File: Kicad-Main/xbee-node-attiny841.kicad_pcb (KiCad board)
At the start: 2 copper layers, 58.5 x 58.5 mm, 44 parts, among them P10 CONN_1, P11 CONN_1, P12 CONN_1, P13 CONN_1, P14 CONN_1, P15 CONN_1, P16 CONN_1, P17 CONN_1, P18 CONN_1, P19 CONN_1, P2 XBee Adaptor, P3 Test, P4 Battery, P5 XBee-ext-1, P6 XBee-ext-2, P7 CONN_1, P8 CONN_1, P9 CONN_1, Q2 S9014, Q3 2N7000, U1 ATTINY84-S, U2 MAX952ESA, U3 TPS77033, U4 TPS77033

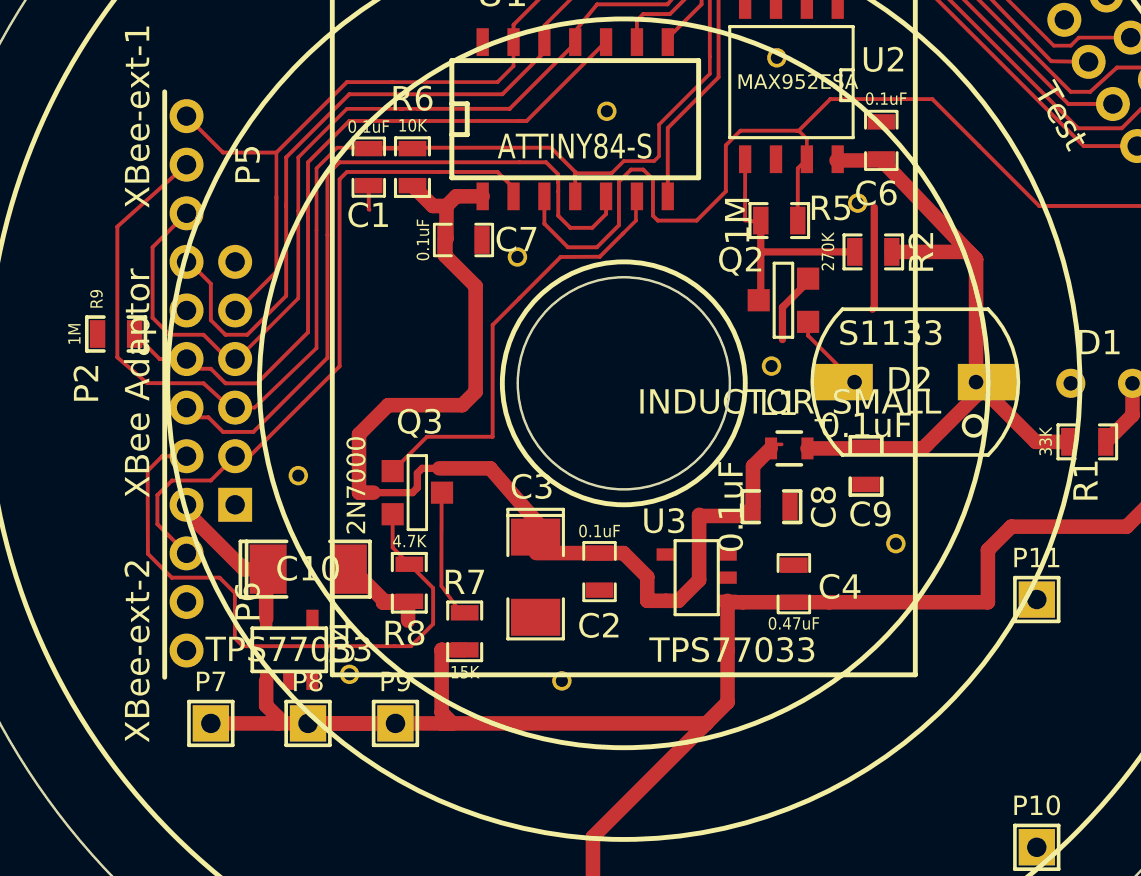
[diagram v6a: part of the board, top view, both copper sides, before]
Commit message: Change PCBs to move XBee regulator and caps to the mount board. Change Vcc on mount board to take full battery voltage.
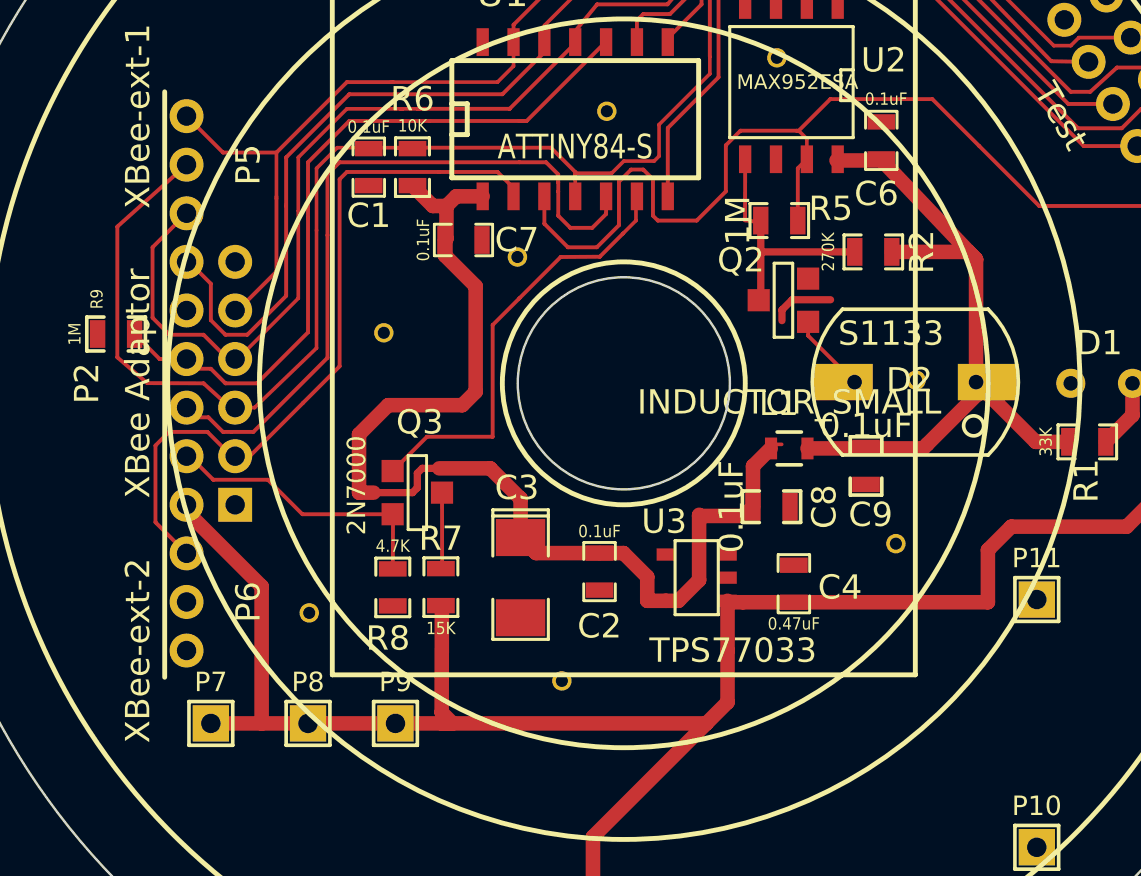
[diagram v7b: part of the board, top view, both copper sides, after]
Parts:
- removed C10: 3.3uF, SMD_Packages:SMD-1206_Pol
- removed P19: CONN_1, Photodiode:THROUGHVIA
- removed U4: TPS77033, SMD_Packages:SOT-23-5
- moved P14 26.3 mm to (212.0, 99.9)
- moved P17 21.6 mm to (187.1, 109.5)
- moved P12 6.85 mm to (190.1, 97.9)
- moved R7 2.07 mm to (192.5, 108.4)
- moved R8 0.71 mm to (190.5, 108.4)
- moved C3 0.62 mm to (195.8, 108.0)
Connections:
- P2 pad 2: /VDDX -> /Battery
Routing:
- net /VBatt: track 25.3 -> 11.9 mm
- net GND: track 13.4 -> 0.04 mm
- net /VDDX: track 7.25 -> 0.00 mm
- net /Battery: track 86.2 -> 90.2 mm
- net /Reset: track 77.9 -> 75.0 mm
- net (no net): track 0.00 -> 2.61 mm
- net /VDDA: track 31.8 -> 29.4 mm
- net /Bootloader: track 28.2 -> 30.3 mm
- net Net-(Q3-PadD): track 5.26 -> 3.25 mm
- net VDD: track 45.6 -> 46.7 mm
